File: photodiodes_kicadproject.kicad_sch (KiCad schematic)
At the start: 0 parts

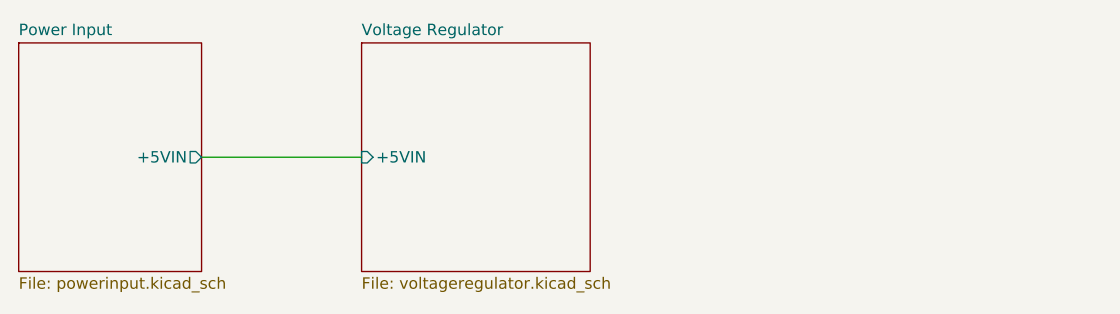
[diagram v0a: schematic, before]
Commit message: Added photodiode circuit.
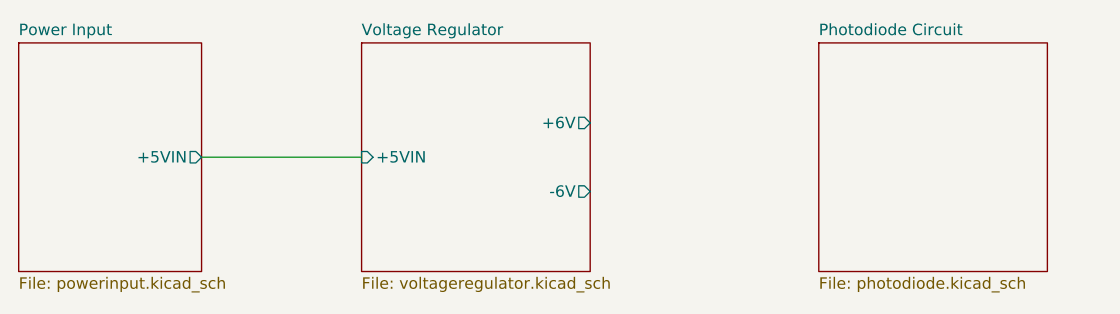
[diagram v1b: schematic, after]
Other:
- added sheet Photodiode Circuit (photodiode.kicad_sch)
- sheet Voltage Regulator ports: added +6V, -6V; removed none
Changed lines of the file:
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@@
+	)
+	(sheet
+		(at 165.1 76.2)
+		(size 25.4 25.4)
+		(exclude_from_sim no)
+		(in_bom yes)
+		(on_board yes)
+		(dnp no)
+		(fields_autoplaced yes)
+		(stroke
+			(width 0.1524)
+			(type solid)
+		)
+		(fill
+			(color 37 255 132 1)
+		)
+		(property "Sheetname" "Photodiode Circuit"
+			(at 165.1 75.4884 0)
+			(show_name no)
+			(do_not_autoplace no)
+			(effects
+				(font
+					(size 1.27 1.27)
+				)
+				(justify left bottom)
+			)
+		)
+		(property "Sheetfile" "photodiode.kicad_sch"
+			(at 165.1 102.1846 0)
+			(show_name no)
+			(do_not_autoplace no)
+			(effects
+				(font
+					(size 1.27 1.27)
+				)
+				(justify left top)
+			)
+		)
+		(instances
+			(project "photodiodes_kicadproject"
+				(path "/34628f3a-efff-4ff7-8718-bbff2513d117"
+					(page "4")
+				)
+			)
+		)
 	)
 	(sheet
@@
 			)
 		)
+		(pin "+6V" output
+			(at 139.7 85.09 0)
+			(effects
+				(font
+					(size 1.27 1.27)
+				)
+				(justify right)
+			)
+		)
+		(pin "-6V" output
+			(at 139.7 92.71 0)
+			(effects
+				(font
+					(size 1.27 1.27)
+				)
+				(justify right)
+			)
+		)

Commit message: Save progress.
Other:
- sheet Power Input ports: added +12VIN; removed +5VIN
- sheet Voltage Regulator ports: added +12V; removed +5VIN, +6V, -6V
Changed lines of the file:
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@@
 			)
 		)
-		(pin "+5VIN" input
+		(pin "+12V" input
 			(at 114.3 88.9 180)
 			(effects
@@
 				)
 				(justify left)
-			)
-		)
-		(pin "+6V" output
-			(at 139.7 85.09 0)
-			(effects
-				(font
-					(size 1.27 1.27)
-				)
-				(justify right)
-			)
-		)
-		(pin "-6V" output
-			(at 139.7 92.71 0)
-			(effects
-				(font
-					(size 1.27 1.27)
-				)
-				(justify right)
 			)
 		)
@@
 			)
 		)
-		(pin "+5VIN" output
+		(pin "+12VIN" output
 			(at 96.52 88.9 0)
 			(effects
